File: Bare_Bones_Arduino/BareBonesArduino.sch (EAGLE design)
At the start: 15 parts, among them U1 ATMEGA328P_PDIP

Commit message: Version 2 smaller design
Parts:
- removed JP3: AVR_SPI_PRG_6PTH, SparkFun-Connectors:AVR_SPI_PRG_6PTH
- added JP5: (no value), SparkFun-Connectors:M06SILK_FEMALE_PTH
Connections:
- net GND: now also JP5.1; no longer JP3.6
- net MISO: now also JP5.3; no longer JP3.1
- net MOSI: now also JP5.2; no longer JP3.4
- net RESET: now also JP5.6; no longer JP3.5
- net SCK: now also JP5.4; no longer JP3.3
- net VCC: now also JP5.5; no longer JP3.2

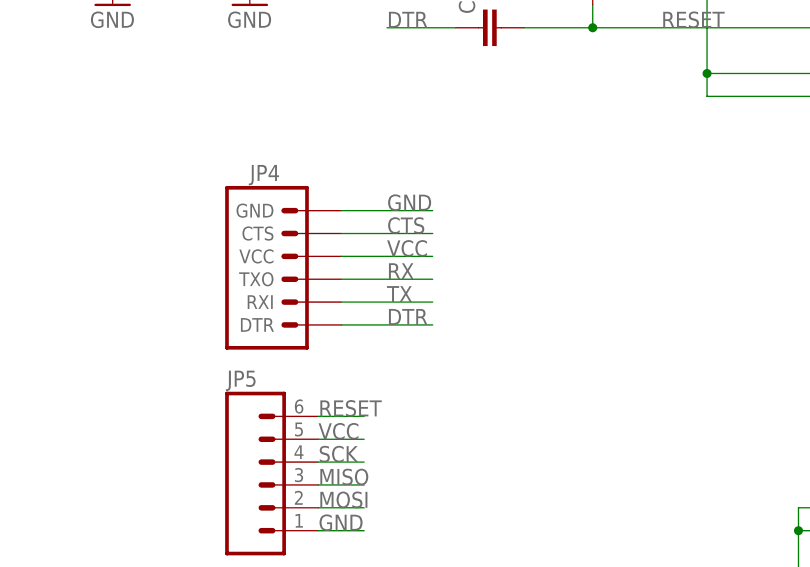
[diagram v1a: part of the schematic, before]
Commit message: Version 2.  Forgot Silks, fix TX/RX
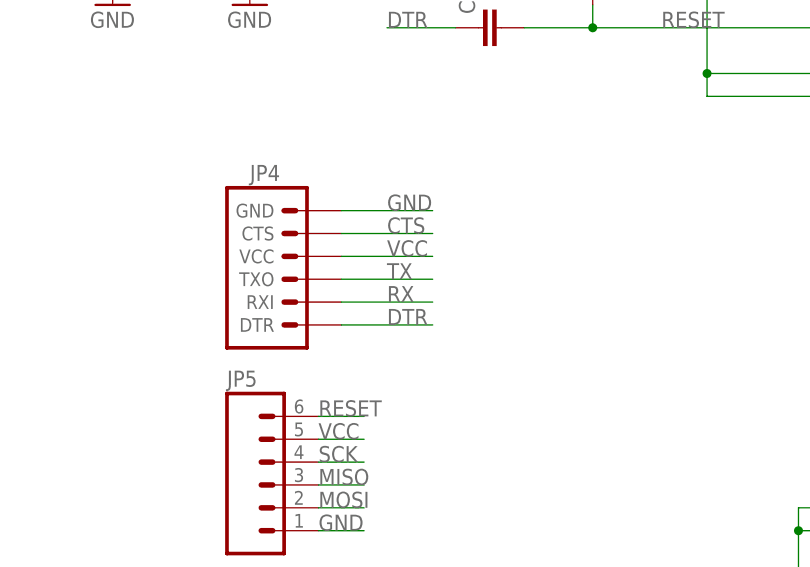
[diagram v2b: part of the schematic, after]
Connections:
- net RX: now also JP4.RXI; no longer JP4.TXO
- net TX: now also JP4.TXO; no longer JP4.RXI
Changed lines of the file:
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@@
 <net name="RX" class="0">
+<segment>
+<pinref part="U1" gate="G$1" pin="PD0(RXD)"/>
+<wire x1="142.24" y1="99.06" x2="149.86" y2="99.06" width="0.1524" layer="91"/>
+<label x="147.32" y="99.06" size="1.778" layer="95"/>
+</segment>
+<segment>
+<pinref part="JP4" gate="G$1" pin="RXI"/>
+<wire x1="38.1" y1="91.44" x2="48.26" y2="91.44" width="0.1524" layer="91"/>
+<label x="43.18" y="91.44" size="1.778" layer="95"/>
+</segment>
+</net>
+<net name="TX" class="0">
+<segment>
+<pinref part="U1" gate="G$1" pin="PD1(TXD)"/>
+<wire x1="142.24" y1="96.52" x2="149.86" y2="96.52" width="0.1524" layer="91"/>
+<label x="147.32" y="96.52" size="1.778" layer="95"/>
+</segment>
 <segment>
 <pinref part="JP4" gate="G$1" pin="TXO"/>
@@
 <label x="43.18" y="93.98" size="1.778" layer="95"/>
 </segment>
-<segment>
-<pinref part="U1" gate="G$1" pin="PD0(RXD)"/>
-<wire x1="142.24" y1="99.06" x2="149.86" y2="99.06" width="0.1524" layer="91"/>
-<label x="147.32" y="99.06" size="1.778" layer="95"/>
-</segment>
 </net>
-<net name="TX" class="0">
-<segment>
-<pinref part="JP4" gate="G$1" pin="RXI"/>
-<wire x1="38.1" y1="91.44" x2="48.26" y2="91.44" width="0.1524" layer="91"/>
-<label x="43.18" y="91.44" size="1.778" layer="95"/>
-</segment>
-<segment>
-<pinref part="U1" gate="G$1" pin="PD1(TXD)"/>
-<wire x1="142.24" y1="96.52" x2="149.86" y2="96.52" width="0.1524" layer="91"/>
-<label x="147.32" y="96.52" size="1.778" layer="95"/>
-</segment>
-</net>
